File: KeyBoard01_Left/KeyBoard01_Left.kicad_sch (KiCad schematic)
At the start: 0 parts

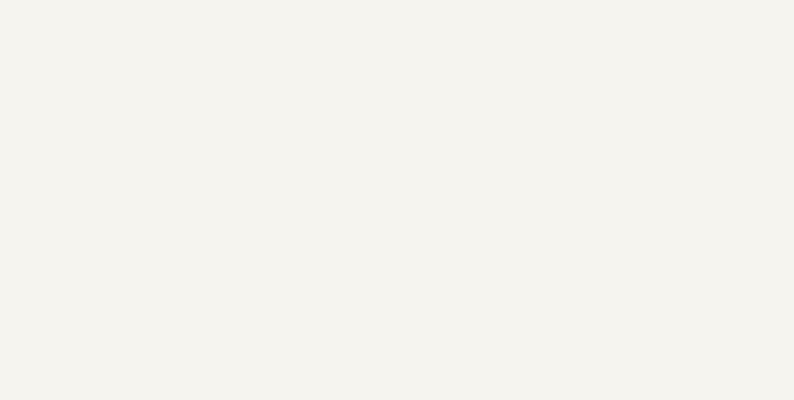
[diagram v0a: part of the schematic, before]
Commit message: PRJ: Update prj to KiCAD 7
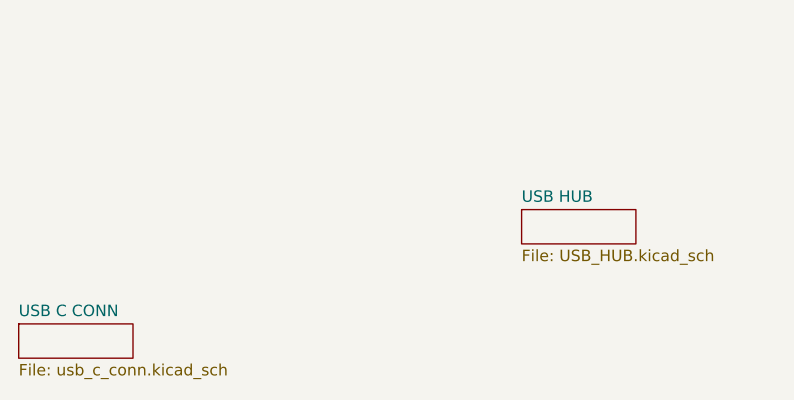
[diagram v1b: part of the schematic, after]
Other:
- added sheet USB C CONN (usb_c_conn.kicad_sch)
- added sheet USB HUB (USB_HUB.kicad_sch)
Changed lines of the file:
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@@
-(kicad_sch (version 20211123) (generator eeschema)
+(kicad_sch (version 20230121) (generator eeschema)
   (paper "A4")
   (sheet (at 200.7108 48.4632) (size 36.5252 32.9692) (fields_autoplaced)
-    (stroke (width 0.1524) (type solid) (color 0 0 0 0))
+    (stroke (width 0.1524) (type solid))
     (fill (color 0 0 0 0.0000))
-    (property "Sheet name" "MCU" (id 0) (at 200.7108 47.7516 0)
+    (property "Sheetname" "MCU" (at 200.7108 47.7516 0)
       (effects (font (size 1.27 1.27)) (justify left bottom))
     )
-    (property "Sheet file" "mcu.kicad_sch" (id 1) (at 200.7108 82.017 0)
+    (property "Sheetfile" "mcu.kicad_sch" (at 200.7108 82.017 0)
       (effects (font (size 1.27 1.27)) (justify left top))
+    )
+    (instances
+      (project "KeyBoard01_Left"
+        (path "/30001e54-b931-4c99-a85a-cc67ed27d667" (page "2"))
+      )
+    )
+  )
+  (sheet (at 163.83 138.43) (size 12.7 3.81) (fields_autoplaced)
+    (stroke (width 0.1524) (type solid))
+    (fill (color 0 0 0 0.0000))
+    (property "Sheetname" "USB C CONN" (at 163.83 137.7184 0)
+      (effects (font (size 1.27 1.27)) (justify left bottom))
+    )
+    (property "Sheetfile" "usb_c_conn.kicad_sch" (at 163.83 142.8246 0)
+      (effects (font (size 1.27 1.27)) (justify left top))
+    )
+    (instances
+      (project "KeyBoard01_Left"
+        (path "/30001e54-b931-4c99-a85a-cc67ed27d667" (page "4"))
+      )
+    )
+  )
+  (sheet (at 219.71 125.73) (size 12.7 3.81) (fields_autoplaced)
+    (stroke (width 0.1524) (type solid))
+    (fill (color 0 0 0 0.0000))
+    (property "Sheetname" "USB HUB" (at 219.71 125.0184 0)
+      (effects (font (size 1.27 1.27)) (justify left bottom))
+    )
+    (property "Sheetfile" "USB_HUB.kicad_sch" (at 219.71 130.1246 0)
+      (effects (font (size 1.27 1.27)) (justify left top))
+    )
+    (instances
+      (project "KeyBoard01_Left"
+        (path "/30001e54-b931-4c99-a85a-cc67ed27d667" (page "3"))
+      )
     )
   )
   (sheet_instances
     (path "/" (page "1"))
-    (path "/3eed219e-ef44-46a2-a482-b7191acccc64" (page "2"))
-  )
-  (symbol_instances
-    (path "/3eed219e-ef44-46a2-a482-b7191acccc64/01b2e235-a990-46d0-9a67-87f3009976a8"
-      (reference "U1") (unit 1) (value "~") (footprint "")
-    )
   )
 )

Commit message: KiCAD prk: update params and pages
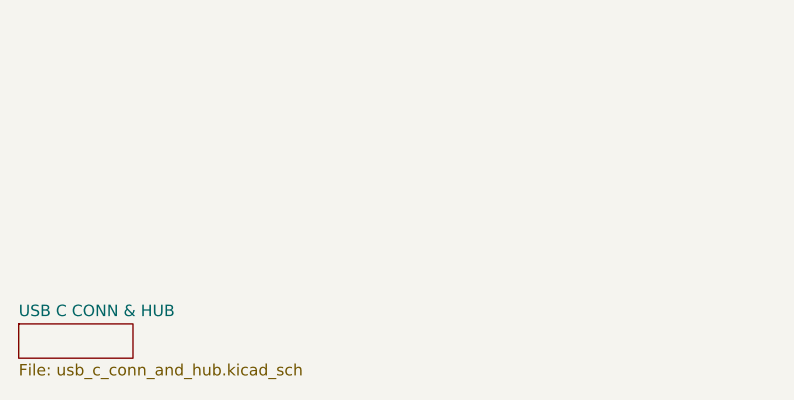
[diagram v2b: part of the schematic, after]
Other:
- sheet USB C CONN renamed USB C CONN & HUB
- removed sheet USB HUB
- sheet USB C CONN & HUB: file usb_c_conn.kicad_sch -> usb_c_conn_and_hub.kicad_sch
- company: (none) -> Embedded Dojo
- title: (none) -> Block Diagram
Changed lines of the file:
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@@
 (kicad_sch (version 20230121) (generator eeschema)
   (paper "A4")
+  (title_block
+    (title "Block Diagram")
+    (company "Embedded Dojo")
+    (comment 1 "imuguruza and hans")
+  )
   (sheet (at 200.7108 48.4632) (size 36.5252 32.9692) (fields_autoplaced)
     (stroke (width 0.1524) (type solid))
@@
     (stroke (width 0.1524) (type solid))
     (fill (color 0 0 0 0.0000))
-    (property "Sheetname" "USB C CONN" (at 163.83 137.7184 0)
+    (property "Sheetname" "USB C CONN & HUB" (at 163.83 137.7184 0)
       (effects (font (size 1.27 1.27)) (justify left bottom))
     )
-    (property "Sheetfile" "usb_c_conn.kicad_sch" (at 163.83 142.8246 0)
+    (property "Sheetfile" "usb_c_conn_and_hub.kicad_sch" (at 163.83 142.8246 0)
       (effects (font (size 1.27 1.27)) (justify left top))
     )
@@
       )
     )
-  )
-  (sheet (at 219.71 125.73) (size 12.7 3.81) (fields_autoplaced)
-    (stroke (width 0.1524) (type solid))
-    (fill (color 0 0 0 0.0000))
-    (property "Sheetname" "USB HUB" (at 219.71 125.0184 0)
-      (effects (font (size 1.27 1.27)) (justify left bottom))
-    )
-    (property "Sheetfile" "USB_HUB.kicad_sch" (at 219.71 130.1246 0)
-      (effects (font (size 1.27 1.27)) (justify left top))
-    )
-    (instances
-      (project "KeyBoard01_Left"
-        (path "/30001e54-b931-4c99-a85a-cc67ed27d667" (page "3"))
-      )
-    )

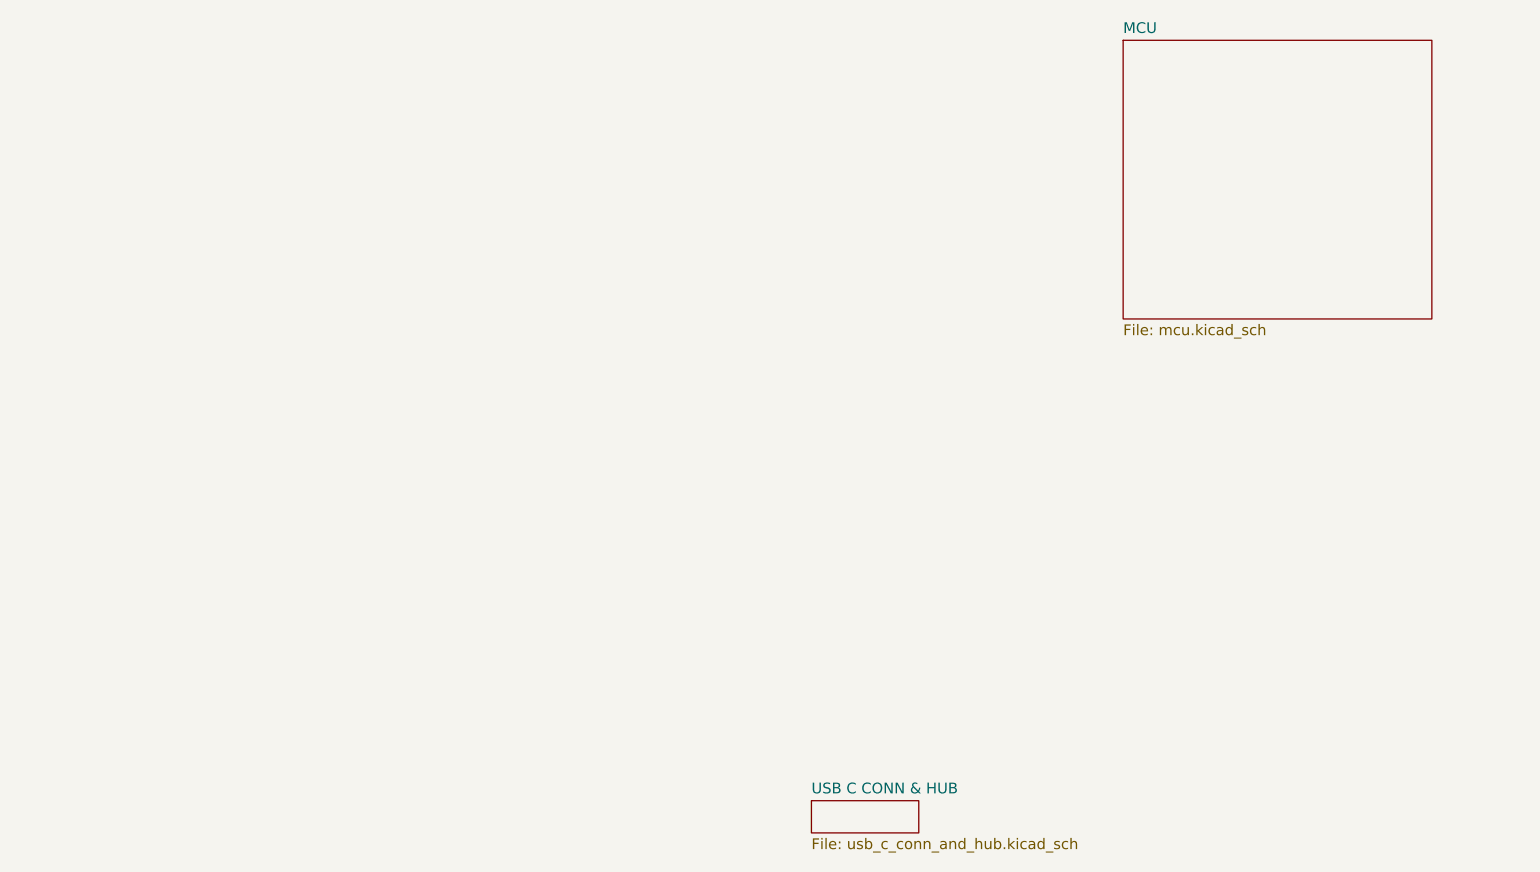
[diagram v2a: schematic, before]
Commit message: KiCAD PRJ: Update and add new signals and sheets
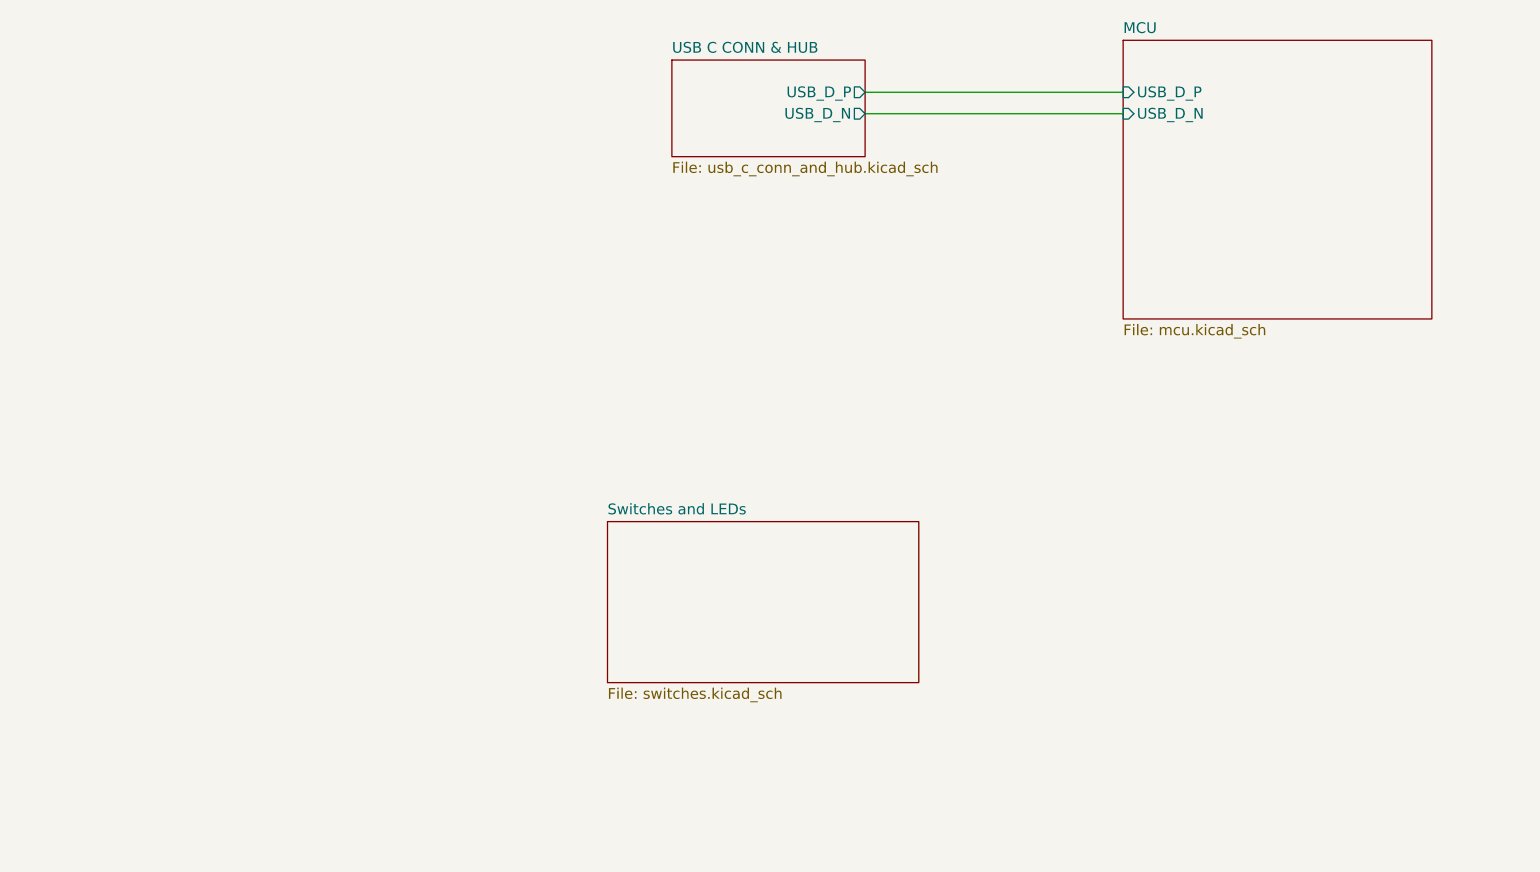
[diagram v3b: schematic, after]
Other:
- added sheet Switches and LEDs (switches.kicad_sch)
- sheet MCU ports: added USB_D_N, USB_D_P; removed none
- sheet USB C CONN & HUB ports: added USB_D_N, USB_D_P; removed none
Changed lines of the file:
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@@
     (comment 1 "imuguruza and hans")
+  )
+  (wire (pts (xy 170.18 57.15) (xy 200.66 57.15))
+    (stroke (width 0) (type default))
+  )
+  (wire (pts (xy 170.18 54.61) (xy 200.66 54.61))
+    (stroke (width 0) (type default))
   )
   (sheet (at 200.7108 48.4632) (size 36.5252 32.9692) (fields_autoplaced)
@@
       (effects (font (size 1.27 1.27)) (justify left top))
     )
+    (pin "USB_D_N" input (at 200.7108 57.15 180)
+      (effects (font (size 1.27 1.27)) (justify left))
+    )
+    (pin "USB_D_P" input (at 200.7108 54.61 180)
+      (effects (font (size 1.27 1.27)) (justify left))
+    )
     (instances
       (project "KeyBoard01_Left"
@@
     )
   )
-  (sheet (at 163.83 138.43) (size 12.7 3.81) (fields_autoplaced)
+  (sheet (at 147.32 50.8) (size 22.86 11.43) (fields_autoplaced)
     (stroke (width 0.1524) (type solid))
     (fill (color 0 0 0 0.0000))
-    (property "Sheetname" "USB C CONN & HUB" (at 163.83 137.7184 0)
+    (property "Sheetname" "USB C CONN & HUB" (at 147.32 50.0884 0)
       (effects (font (size 1.27 1.27)) (justify left bottom))
     )
-    (property "Sheetfile" "usb_c_conn_and_hub.kicad_sch" (at 163.83 142.8246 0)
+    (property "Sheetfile" "usb_c_conn_and_hub.kicad_sch" (at 147.32 62.8146 0)
       (effects (font (size 1.27 1.27)) (justify left top))
     )
+    (pin "USB_D_P" output (at 170.18 54.61 0)
+      (effects (font (size 1.27 1.27)) (justify right))
+    )
+    (pin "USB_D_N" output (at 170.18 57.15 0)
+      (effects (font (size 1.27 1.27)) (justify right))
+    )
+    (instances
+      (project "KeyBoard01_Left"
+        (path "/30001e54-b931-4c99-a85a-cc67ed27d667" (page "4"))
+      )
+    )
+  )
+  (sheet (at 139.7 105.41) (size 36.83 19.05) (fields_autoplaced)
+    (stroke (width 0.1524) (type solid))
+    (fill (color 0 0 0 0.0000))
+    (property "Sheetname" "Switches and LEDs" (at 139.7 104.6984 0)
+      (effects (font (size 1.27 1.27)) (justify left bottom))
+    )
+    (property "Sheetfile" "switches.kicad_sch" (at 139.7 125.0446 0)
+      (effects (font (size 1.27 1.27)) (justify left top))
+    )

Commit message: SCH Hierarchy: Add LEDs sheet and add ports to entries
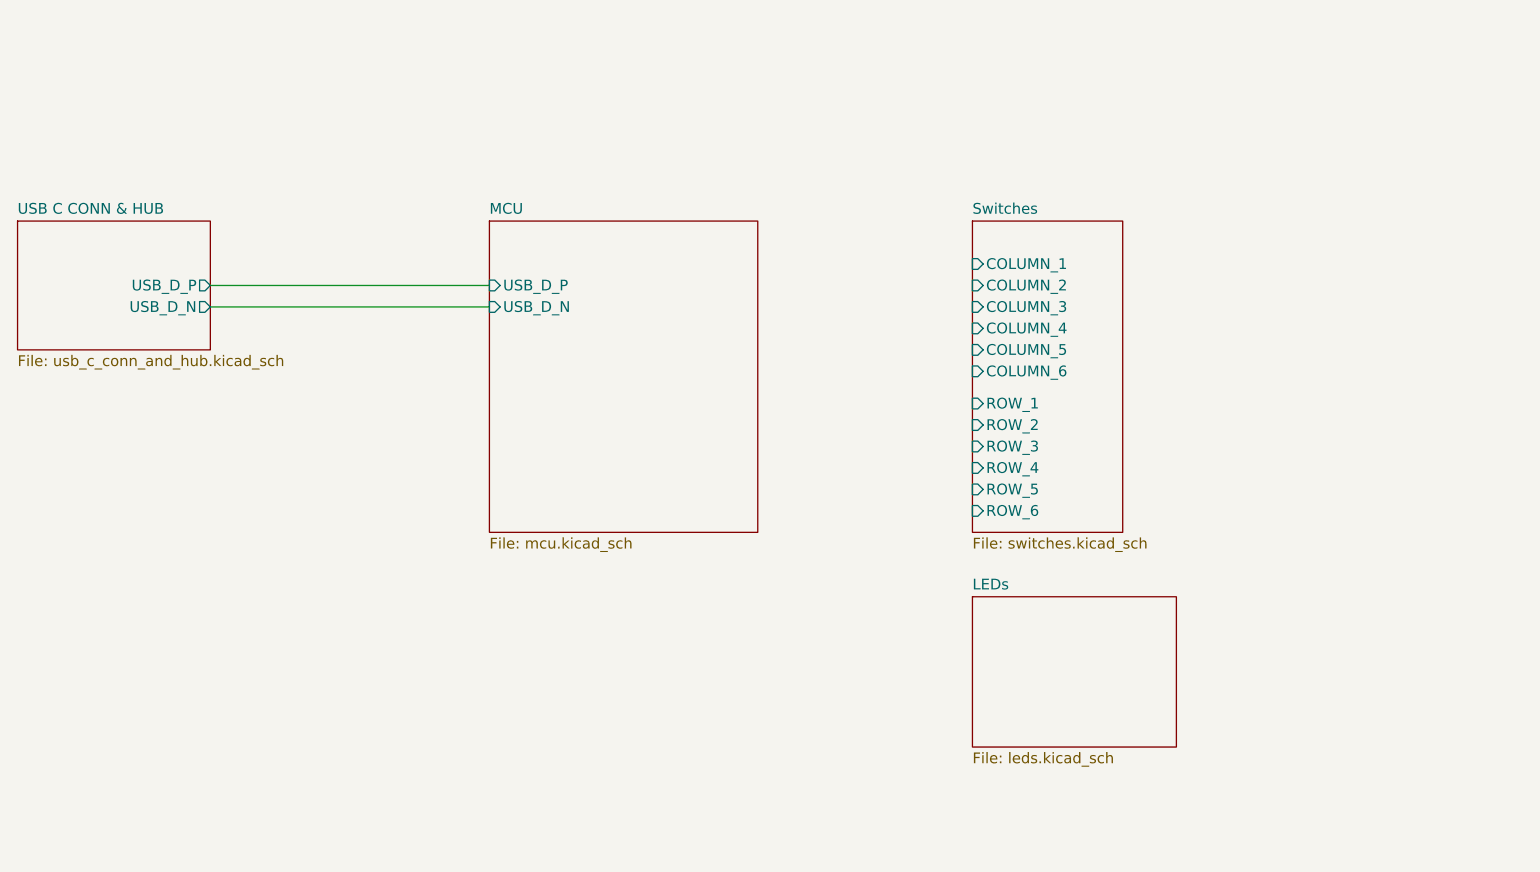
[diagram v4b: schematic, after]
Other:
- sheet Switches and LEDs renamed Switches
- added sheet LEDs (leds.kicad_sch)
- sheet Switches ports: added COLUMN_1, COLUMN_2, COLUMN_3, COLUMN_4, COLUMN_5, COLUMN_6, ROW_1, ROW_2, ROW_3, ROW_4, ROW_5, ROW_6; removed none
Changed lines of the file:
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@@
     (comment 1 "imuguruza and hans")
   )
-  (wire (pts (xy 170.18 57.15) (xy 200.66 57.15))
+  (wire (pts (xy 92.71 80.01) (xy 125.6792 80.01))
     (stroke (width 0) (type default))
   )
-  (wire (pts (xy 170.18 54.61) (xy 200.66 54.61))
+  (wire (pts (xy 92.71 77.47) (xy 125.6792 77.47))
     (stroke (width 0) (type default))
   )
-  (sheet (at 200.7108 48.4632) (size 36.5252 32.9692) (fields_autoplaced)
+  (sheet (at 125.73 69.85) (size 31.75 36.83) (fields_autoplaced)
     (stroke (width 0.1524) (type solid))
     (fill (color 0 0 0 0.0000))
-    (property "Sheetname" "MCU" (at 200.7108 47.7516 0)
+    (property "Sheetname" "MCU" (at 125.73 69.1384 0)
       (effects (font (size 1.27 1.27)) (justify left bottom))
     )
-    (property "Sheetfile" "mcu.kicad_sch" (at 200.7108 82.017 0)
+    (property "Sheetfile" "mcu.kicad_sch" (at 125.73 107.2646 0)
       (effects (font (size 1.27 1.27)) (justify left top))
     )
-    (pin "USB_D_N" input (at 200.7108 57.15 180)
+    (pin "USB_D_N" input (at 125.73 80.01 180)
       (effects (font (size 1.27 1.27)) (justify left))
     )
-    (pin "USB_D_P" input (at 200.7108 54.61 180)
+    (pin "USB_D_P" input (at 125.73 77.47 180)
       (effects (font (size 1.27 1.27)) (justify left))
     )
@@
     )
   )
-  (sheet (at 147.32 50.8) (size 22.86 11.43) (fields_autoplaced)
+  (sheet (at 182.88 114.3) (size 24.13 17.78) (fields_autoplaced)
     (stroke (width 0.1524) (type solid))
     (fill (color 0 0 0 0.0000))
-    (property "Sheetname" "USB C CONN & HUB" (at 147.32 50.0884 0)
+    (property "Sheetname" "LEDs" (at 182.88 113.5884 0)
       (effects (font (size 1.27 1.27)) (justify left bottom))
     )
-    (property "Sheetfile" "usb_c_conn_and_hub.kicad_sch" (at 147.32 62.8146 0)
+    (property "Sheetfile" "leds.kicad_sch" (at 182.88 132.6646 0)
       (effects (font (size 1.27 1.27)) (justify left top))
     )
-    (pin "USB_D_P" output (at 170.18 54.61 0)
+    (instances
+      (project "KeyBoard01_Left"
+        (path "/30001e54-b931-4c99-a85a-cc67ed27d667" (page "5"))
+      )
+    )
+  )
+  (sheet (at 69.9008 69.85) (size 22.8092 15.24) (fields_autoplaced)
+    (stroke (width 0.1524) (type solid))
+    (fill (color 0 0 0 0.0000))
+    (property "Sheetname" "USB C CONN & HUB" (at 69.9008 69.1384 0)
+      (effects (font (size 1.27 1.27)) (justify left bottom))
+    )
+    (property "Sheetfile" "usb_c_conn_and_hub.kicad_sch" (at 69.9008 85.6746 0)
+      (effects (font (size 1.27 1.27)) (justify left top))
+    )
+    (pin "USB_D_P" output (at 92.71 77.47 0)
       (effects (font (size 1.27 1.27)) (justify right))
     )
-    (pin "USB_D_N" output (at 170.18 57.15 0)
+    (pin "USB_D_N" output (at 92.71 80.01 0)
       (effects (font (size 1.27 1.27)) (justify right))
     )
@@
     )
   )
-  (sheet (at 139.7 105.41) (size 36.83 19.05) (fields_autoplaced)
+  (sheet (at 182.88 69.85) (size 17.78 36.83) (fields_autoplaced)
     (stroke (width 0.1524) (type solid))
     (fill (color 0 0 0 0.0000))
-    (property "Sheetname" "Switches and LEDs" (at 139.7 104.6984 0)
+    (property "Sheetname" "Switches" (at 182.88 69.1384 0)
       (effects (font (size 1.27 1.27)) (justify left bottom))
     )
-    (property "Sheetfile" "switches.kicad_sch" (at 139.7 125.0446 0)
+    (property "Sheetfile" "switches.kicad_sch" (at 182.88 107.2646 0)
       (effects (font (size 1.27 1.27)) (justify left top))
     )
+    (pin "ROW_6" input (at 182.88 104.14 180)
+      (effects (font (size 1.27 1.27)) (justify left))
+    )
+    (pin "ROW_5" input (at 182.88 101.6 180)
+      (effects (font (size 1.27 1.27)) (justify left))
+    )
+    (pin "COLUMN_1" input (at 182.88 74.93 180)
+      (effects (font (size 1.27 1.27)) (justify left))
+    )
+    (pin "ROW_1" input (at 182.88 91.44 180)
+      (effects (font (size 1.27 1.27)) (justify left))
+    )
+    (pin "ROW_2" input (at 182.88 93.98 180)
+      (effects (font (size 1.27 1.27)) (justify left))
+    )
+    (pin "ROW_3" input (at 182.88 96.52 180)
+      (effects (font (size 1.27 1.27)) (justify left))
+    )
+    (pin "ROW_4" input (at 182.88 99.06 180)
+      (effects (font (size 1.27 1.27)) (justify left))
+    )
+    (pin "COLUMN_4" input (at 182.88 82.55 180)
+      (effects (font (size 1.27 1.27)) (justify left))
+    )
+    (pin "COLUMN_3" input (at 182.88 80.01 180)
+      (effects (font (size 1.27 1.27)) (justify left))
+    )
+    (pin "COLUMN_2" input (at 182.88 77.47 180)
+      (effects (font (size 1.27 1.27)) (justify left))
+    )
+    (pin "COLUMN_5" input (at 182.88 85.09 180)
+      (effects (font (size 1.27 1.27)) (justify left))
+    )
+    (pin "COLUMN_6" input (at 182.88 87.63 180)
+      (effects (font (size 1.27 1.27)) (justify left))
+    )
     (instances
